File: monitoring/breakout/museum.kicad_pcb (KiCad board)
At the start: 2 copper layers, 59.7 x 39.4 mm, 15 parts, among them CON1 UNREG_VIN, J1 RJ45_TRACER, P1 CONN_13X2, P2 I2C_2, P3 I2C_1, P4 12V_LOAD, P5 5V_LOAD, Q1 IRFZ44N, Q2 IRFZ44N, U1 LM7812CT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

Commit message: Updates board
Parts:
- removed the REF** at (181.9, 115.8)
- added REF**: Symbol_OSHW-Logo_SilkScreen, Symbols:Symbol_OSHW-Logo_SilkScreen, F.Cu at (181.9, 116.1)
- U2, U3: footprint Converters_DCDC_ACDC:DCDC-Conv_Recom_R-78HBxx-0.5 -> dc_dc:RECOM_R-78xx
- moved U2 2.65 mm to (151.9, 104.1)
- moved U3 2.65 mm to (141.7, 104.1)
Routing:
- net GND: track 158.3 -> 139.6 mm
- net 12V_BATT: track 37.0 -> 29.0 mm
- net RASPI_5V: track 16.6 -> 19.1 mm

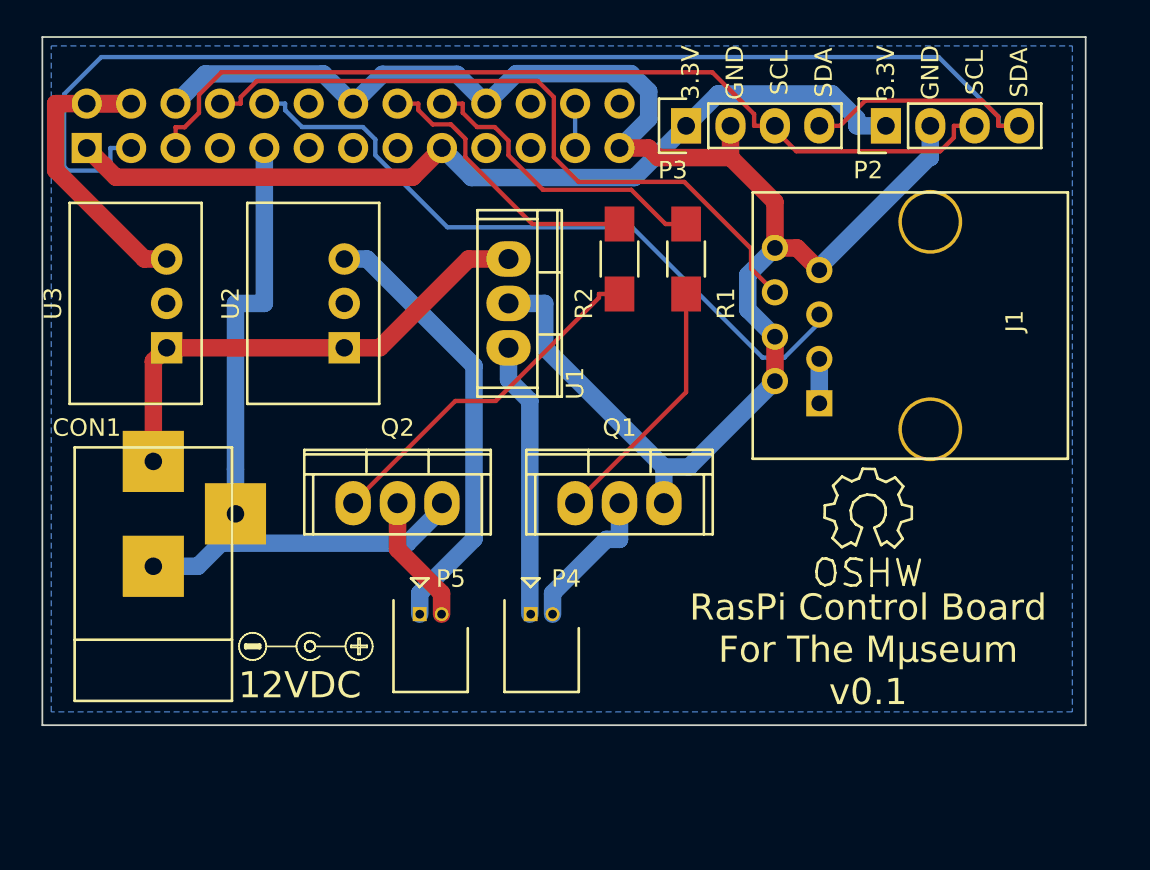
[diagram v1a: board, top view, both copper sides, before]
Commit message: Control board revisions (v0.2)
* Fix RECOM footprints
* Replace MOSFETs with ones whose gate threshold will work for the 3.3v
  Raspi GPIOs
* Add second 12v MOSFET-switched channel to the Raspi GPIO with PWM
* Output channels: move from tiny connectors to ones that should be
  better suited for higher-power use (also one that has screw terminals)
* Replace barrel jack pad slots (which OSH Park doesn't support) with
  holes
* Made board bigger and relaid parts to fit new connectors
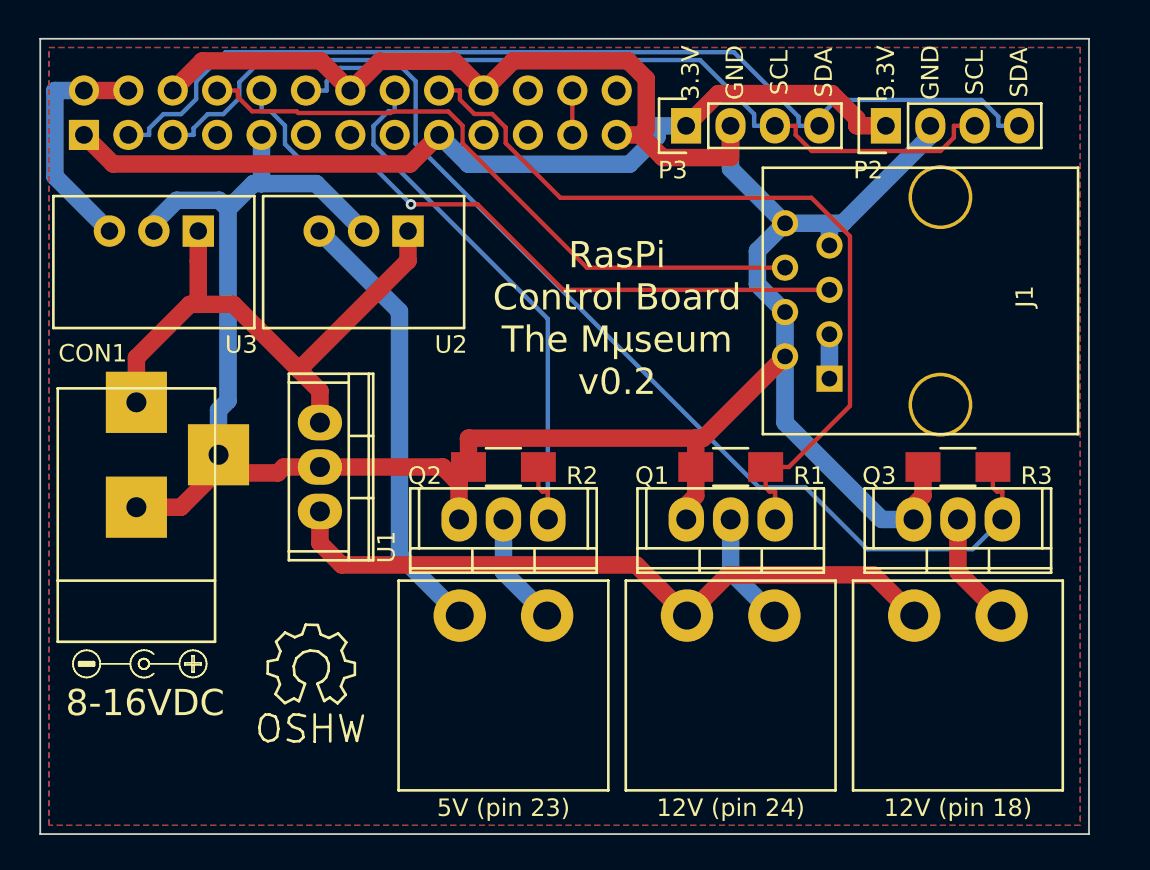
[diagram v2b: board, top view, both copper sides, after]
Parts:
- removed P4: 12V_LOAD, Connectors_Molex:Connector_Molex_PicoBlade_53048-0210
- removed P5: 5V_LOAD, Connectors_Molex:Connector_Molex_PicoBlade_53048-0210
- removed REF**: Symbol_OSHW-Logo_SilkScreen, Symbols:Symbol_OSHW-Logo_SilkScreen
- added 12V (pin 18): 12V_LOAD, connector:OSTOQ027151, F.Cu at (187.0, 126.0)
- added 12V (pin 24): 12V_LOAD, connector:OSTOQ027151, F.Cu at (174.0, 126.0)
- added 5V (pin 23): 5V_LOAD, connector:OSTOQ027151, F.Cu at (161.0, 126.0)
- added ?: , Symbols:Symbol_OSHW-Logo_SilkScreen, F.Cu at (150.0, 125.0)
- added Q3: PSMN022, Power_Integrations:TO-220, F.Cu at (187.0, 116.5)
- added R3: 10K, Resistors_SMD:R_1206_HandSoldering, F.Cu at (187.0, 113.5)
- Q1, Q2: value IRFZ44N -> PSMN022
- moved U1 14.3 mm to (150.5, 113.5)
- moved R2 13.6 mm to (161.0, 113.5), turned to 0 degrees
- moved R1 12.2 mm to (174.0, 113.5), turned to 0 degrees
- moved Q1 6.43 mm to (174.0, 116.5), turned to 180 degrees
- moved Q2 6.13 mm to (161.0, 116.5), turned to 180 degrees
- moved U2 4.29 mm to (153.0, 100.0), turned to 180 degrees
- moved U3 4.20 mm to (141.0, 100.0), turned to 180 degrees
- moved CON1 3.52 mm to (140.0, 116.0)
- moved J1 1.52 mm to (186.0, 104.0)
- moved P1 0.77 mm to (137.0, 94.5)
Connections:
- net TRACER_TXD renamed RASPI_RXD
- Q1 pad 1: Net-(Q1-Pad1) -> RASPI_GPIO_24
- Q1 pad 2: /12V_GND_SW -> Net-(P4-Pad2)
- Q2 pad 1: Net-(Q2-Pad1) -> RASPI_GPIO_23
- R1 pad 1: RASPI_GPIO_24 -> GND
- R1 pad 2: Net-(Q1-Pad1) -> RASPI_GPIO_24
- R2 pad 1: RASPI_GPIO_23 -> GND
- R2 pad 2: Net-(Q2-Pad1) -> RASPI_GPIO_23
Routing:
- net RASPI_GPIO_18: track 0.00 -> 58.3 mm
- net GND: track 139.6 -> 170.4 mm
- net RASPI_GPIO_24: track 17.6 -> 47.2 mm
- net +12V: track 15.8 -> 39.5 mm
- net RASPI_SDA: track 79.6 -> 57.8 mm
- net Net-(Q2-Pad1): track 20.3 -> 0.00 mm
- net RASPI_GPIO_23: track 16.4 -> 32.8 mm
- net Net-(Q1-Pad1): track 14.6 -> 0.00 mm
- net /12V_GND_SW: track 8.38 -> 0.00 mm
- net Net-(P6-Pad2): track 0.00 -> 6.54 mm
- net Net-(P4-Pad2): track 0.00 -> 6.54 mm
- net RASPI_5V: track 19.1 -> 13.5 mm
- net 12V_BATT: track 29.0 -> 32.9 mm
- net RASPI_TXD: track 40.2 -> 37.6 mm
- net RASPI_RXD: track 39.8 -> 38.5 mm, vias 0 -> 1
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- added copper zone on F.Cu, net GND
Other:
- board size 59.7 x 39.4 mm -> 60 x 45.5 mm
- board text added: "8-16VDC"
- board text added: "RasPi Control Board The Mµseum v0.2"
- board text removed: "12VDC"
- board text removed: "RasPi Control Board For The Mµseum v0.1"
